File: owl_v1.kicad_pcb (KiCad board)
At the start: 4 copper layers, 49.7 x 75.8 mm, 63 parts, among them J1 USB_C_Receptacle_USB2.0_16P, J10 JST-PH Battery, J2 SWD, J3 Screw_Terminal_01x03, J4 SPI1_IMU, J5 I2C, J6 Micro_SD_Card_Det_Hirose_DM3AT, J7 I2C OLED, J8 External GPIOs, SW1 SW_SPDT, U1 STM32F103C8T6, U3 FT230XS, U4 SN65HVD230, U5 TLV73333PDBV, Y1 8MHz, Y2 32k768

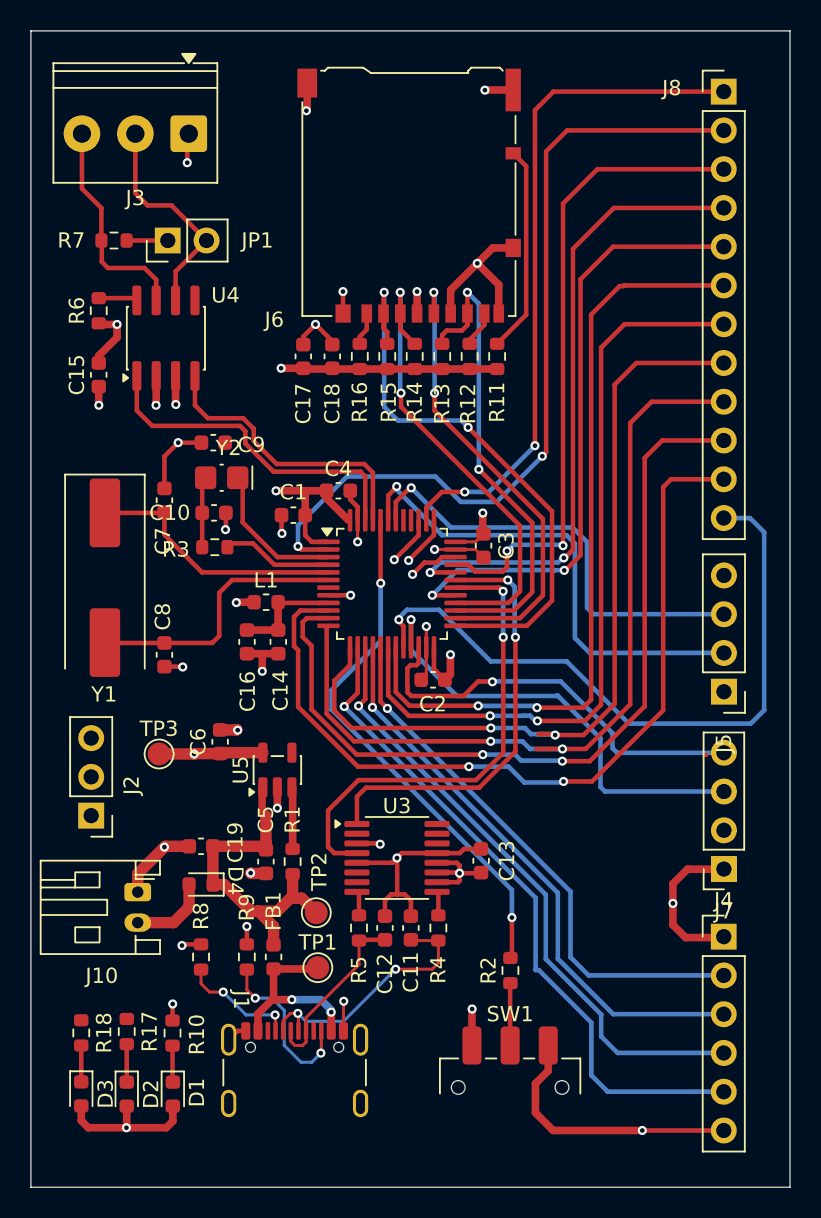
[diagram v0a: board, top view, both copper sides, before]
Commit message: [feat] Add custom design rule check for JLCPCB, finished routing the whole thing, DRC all clear
Taken from here (https://github.com/labtroll/KiCad-DesignRules)
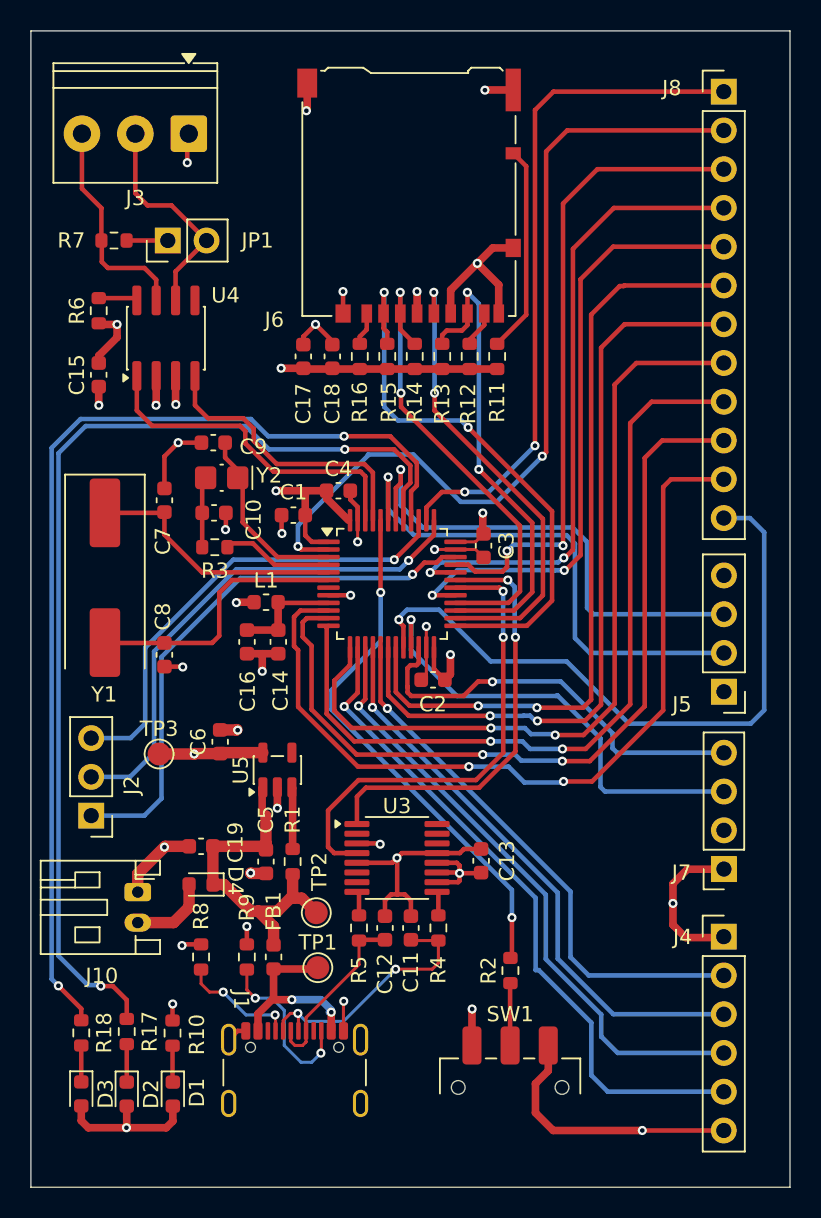
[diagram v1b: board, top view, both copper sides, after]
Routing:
- net LED_GREEN: track 0.00 -> 68.5 mm, vias 0 -> 2
- net LED_BLUE: track 0.00 -> 68.1 mm, vias 0 -> 2
- net SWDIO: track 3.28 -> 36.3 mm
- net SWCLK: track 3.31 -> 33.9 mm
- net TRACE_SWO: track 3.25 -> 30.9 mm
- net I2C_SCLK: track 29.1 -> 32.5 mm
- net LSE_OSC_IN: track 9.49 -> 12.1 mm
- net I2C_SDA: track 32.2 -> 34.5 mm
- net GPIO_7: track 55.3 -> 53.2 mm
- net GPIO_8: track 54.7 -> 53.0 mm
- net GPIO_1: track 55.0 -> 56.2 mm

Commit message: [feat] Add owl logo
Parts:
- added Owl v0.1: LOGO, LOGO, F.Cu at (189.1, 101.8)

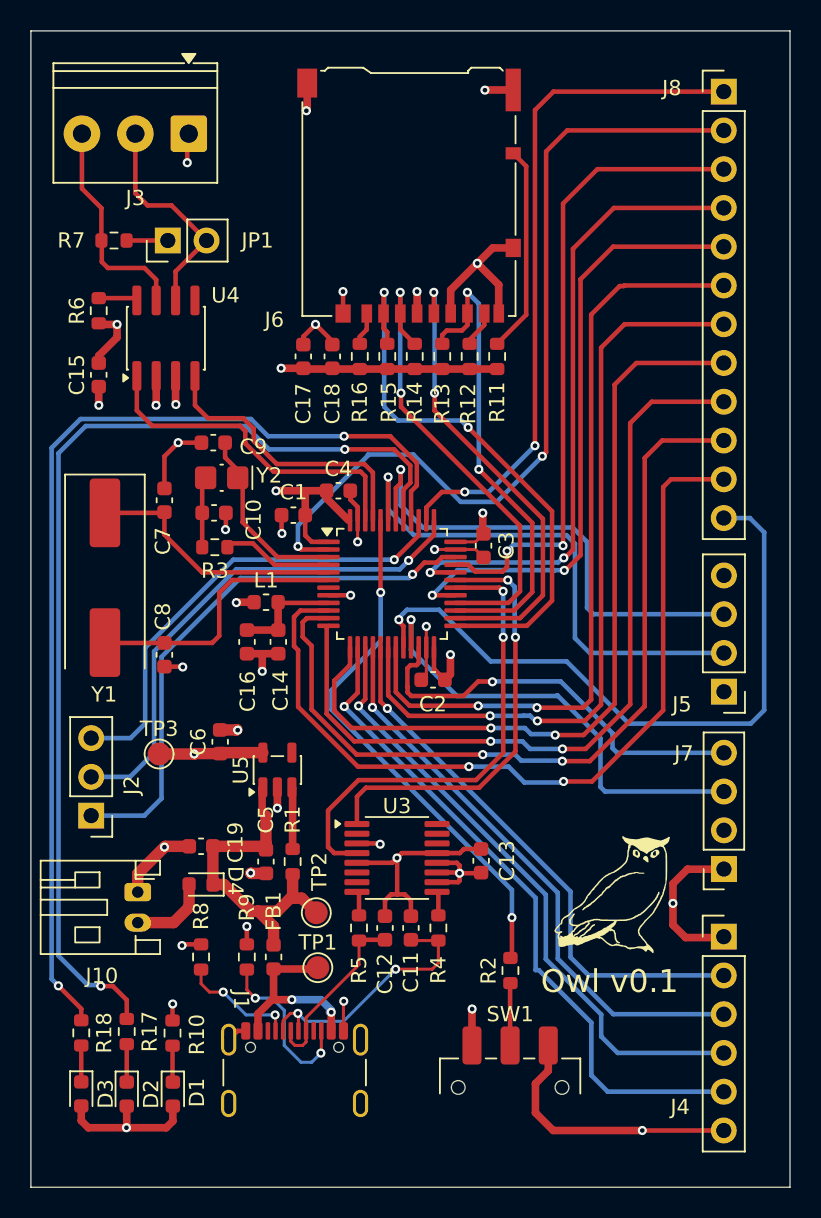
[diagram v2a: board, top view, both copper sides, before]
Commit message: [chore] Add labels with front silkscreen
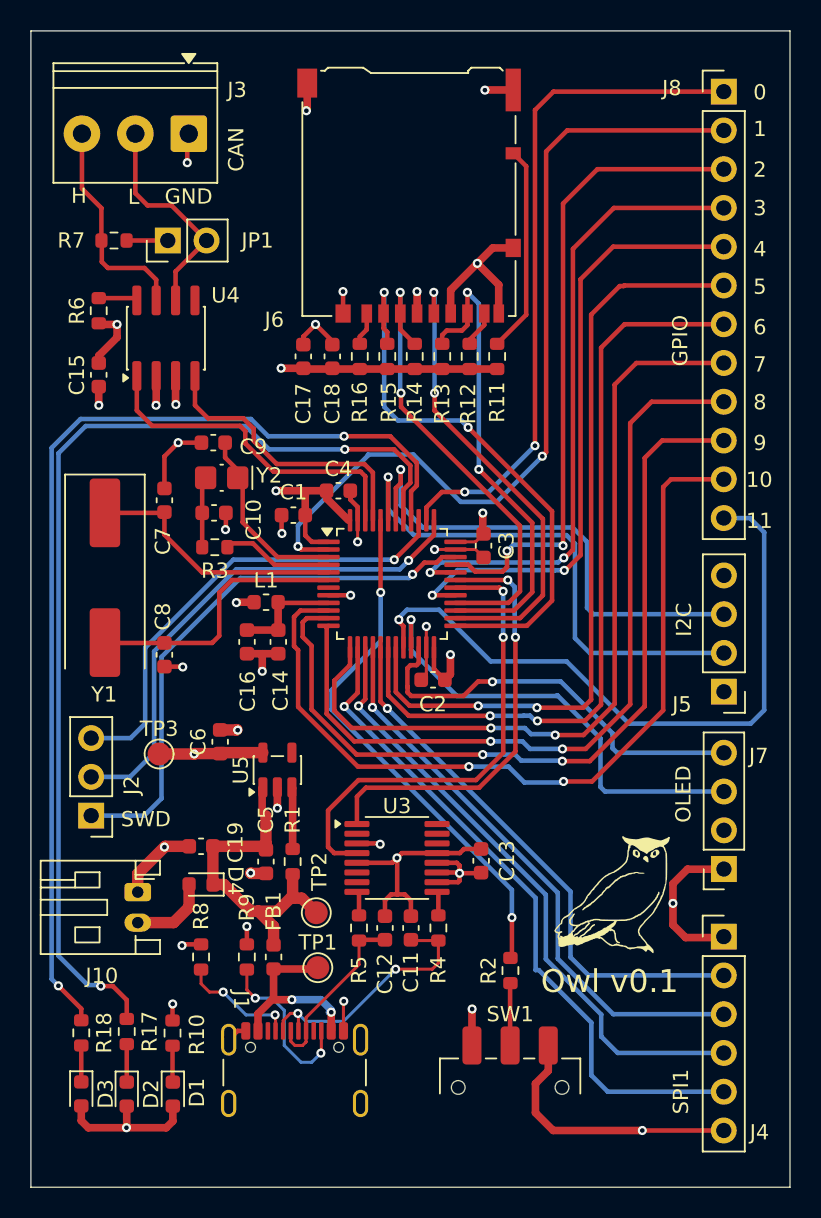
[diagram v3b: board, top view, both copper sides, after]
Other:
- board text added: "0"
- board text added: "1"
- board text added: "10"
- board text added: "11"
- board text added: "2"
- board text added: "3"
- board text added: "4"
- board text added: "5"
- board text added: "6"
- board text added: "7"
- board text added: "8"
- board text added: "9"
- board text added: "CAN"
- board text added: "GND"
- board text added: "GPIO"
- board text added: "H"
- board text added: "I2C"
- board text added: "L"
- board text added: "OLED"
- board text added: "SPI1"
- board text added: "SWD"
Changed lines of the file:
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@@
 		(tags "Through hole socket strip THT 1x04 2.54mm single row")
 		(property "Reference" "J7"
-			(at 2.62 7.57 0)
+			(at -2.28 7.41 0)
 			(layer "F.SilkS")
 			(effects
@@
 		(tags "THT Terminal Block Phoenix PT-1,5-3-3.5-H pitch 3.5mm size 10.5x7.6mm drill 1.2mm pad 2.4mm")
 		(property "Reference" "J3"
-			(at 3.5 -4.22 0)
+			(at -3.165 2.865 0)
 			(layer "F.SilkS")
 			(effects
@@
 		(tags "Through hole pin header THT 1x06 2.54mm single row")
 		(property "Reference" "J4"
-			(at -2.86 11.16 0)
+			(at 2.34 12.82 0)
 			(layer "F.SilkS")
 			(effects
@@
 		(layer "Edge.Cuts")
 	)
+	(gr_text "H\n"
+		(at 153.68 56.66 0)
+		(layer "F.SilkS")
+		(effects
+			(font
+				(size 1 1)
+				(thickness 0.15)
+			)
+			(justify left bottom)
+		)
+	)
+	(gr_text "SWD\n"
+		(at 156.94 97.51 0)
+		(layer "F.SilkS")
+		(effects
+			(font
+				(size 1 1)
+				(thickness 0.15)
+			)
+			(justify left bottom)
+		)
+	)
+	(gr_text "L\n"
+		(at 157.4 56.73 0)
+		(layer "F.SilkS")
+		(effects
+			(font
+				(size 1 1)
+				(thickness 0.15)
+			)
+			(justify left bottom)
+		)
+	)
+	(gr_text "GND"
+		(at 159.81 56.71 0)
+		(layer "F.SilkS")
+		(effects
+			(font
+				(size 1 1)
+				(thickness 0.15)
+			)
+			(justify left bottom)
+		)
+	)
+	(gr_text "10\n"
+		(at 197.903809 75.27 0)
+		(layer "F.SilkS")
+		(effects
+			(font
+				(size 1 1)
+				(thickness 0.15)
+			)
+			(justify left bottom)
+		)
+	)
+	(gr_text "11"
+		(at 197.903809 77.96 0)
+		(layer "F.SilkS")
+		(effects
+			(font
+				(size 1 1)
+				(thickness 0.15)
+			)
+			(justify left bottom)
+		)
+	)
+	(gr_text "0\n"
+		(at 198.38 49.88 0)
+		(layer "F.SilkS")
+		(effects
+			(font
+				(size 1 1)
+				(thickness 0.15)
+			)
+			(justify left bottom)
+		)
+	)
+	(gr_text "1\n"
+		(at 198.38 52.28 0)
+		(layer "F.SilkS")
+		(effects
+			(font
+				(size 1 1)
+				(thickness 0.15)
+			)
+			(justify left bottom)
+		)
+	)
+	(gr_text "2"
+		(at 198.38 54.95 0)
+		(layer "F.SilkS")
+		(effects
+			(font
+				(size 1 1)
+				(thickness 0.15)
+			)
+			(justify left bottom)
+		)
+	)
+	(gr_text "3"
+		(at 198.38 57.47 0)
+		(layer "F.SilkS")
+		(effects
+			(font
+				(size 1 1)
+				(thickness 0.15)
+			)
+			(justify left bottom)
+		)
+	)
+	(gr_text "4"
+		(at 198.38 60.16 0)
+		(layer "F.SilkS")
+		(effects
+			(font
+				(size 1 1)
+				(thickness 0.15)
+			)
+			(justify left bottom)
+		)
+	)
+	(gr_text "5"
+		(at 198.38 62.62 0)
+		(layer "F.SilkS")
+		(effects
+			(font
+				(size 1 1)
+				(thickness 0.15)
+			)
+			(justify left bottom)
+		)
+	)
+	(gr_text "6"
+		(at 198.38 65.27 0)
+		(layer "F.SilkS")
+		(effects
+			(font
+				(size 1 1)
+				(thickness 0.15)
+			)
+			(justify left bottom)
+		)
+	)
+	(gr_text "7"
+		(at 198.38 67.71 0)
+		(layer "F.SilkS")
+		(effects
+			(font
+				(size 1 1)
+				(thickness 0.15)
+			)
+			(justify left bottom)
+		)
+	)
+	(gr_text "8"
+		(at 198.38 70.19 0)
+		(layer "F.SilkS")
+		(effects
+			(font
+				(size 1 1)
+				(thickness 0.15)
+			)
+			(justify left bottom)
+		)
+	)
+	(gr_text "9"
+		(at 198.38 72.86 0)
+		(layer "F.SilkS")
+		(effects
+			(font
+				(size 1 1)
+				(thickness 0.15)
+			)
+			(justify left bottom)
+		)
+	)
+	(gr_text "CAN"
+		(at 165.09 54.5 90)
+		(layer "F.SilkS")
+		(effects
+			(font
+				(size 1 1)
+				(thickness 0.15)
+			)
+			(justify left bottom)
+		)
+	)
+	(gr_text "GPIO"
+		(at 194.18 67.25 90)
+		(layer "F.SilkS")
+		(effects
+			(font
+				(size 1 1)
+				(thickness 0.15)
+			)
+			(justify left bottom)
+		)
+	)
+	(gr_text "SPI1\n"
+		(at 194.23 116.26 90)
+		(layer "F.SilkS")
+		(effects
+			(font
+				(size 1 1)
+				(thickness 0.15)
+			)
+			(justify left bottom)
+		)
+	)
+	(gr_text "OLED"
+		(at 194.39 97.16 90)
+		(layer "F.SilkS")
+		(effects
+			(font
+				(size 1 1)
+				(thickness 0.15)
+			)
+			(justify left bottom)
+		)
+	)
+	(gr_text "I2C"
+		(at 194.43 84.97 90)
+		(layer "F.SilkS")
+		(effects
+			(font
+				(size 1 1)
+				(thickness 0.15)
+			)
+			(justify left bottom)
+		)
+	)
 	(gr_text "D4"
